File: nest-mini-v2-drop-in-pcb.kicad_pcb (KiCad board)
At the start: 4 copper layers, 74.5 x 70.6 mm, 177 parts, among them J1 1775443-2, J2 usb_c, Q1 LBSS138WT1G, Q2 BC847B, SW1 SMXS‑01K‑TP, U1 TPS62130, U10 SN74LVC125APWR, U11 MAX98357AETE_T, U12 FSUSB42MUX, U13 AP22802AW5-7, U2 MIC5365-1.8YC5-TR, U3 TPS62130, U4 MIC5365-0.9YC5-TR, U5 ESP32-S3R8, U6 W25Q128JVSIQ, U7 XU316-1024-QF60B-C24, U8 W25Q128JVSIQ, U9 TLV73333PDBVR, Y1 40MHz, Y2 24MHz

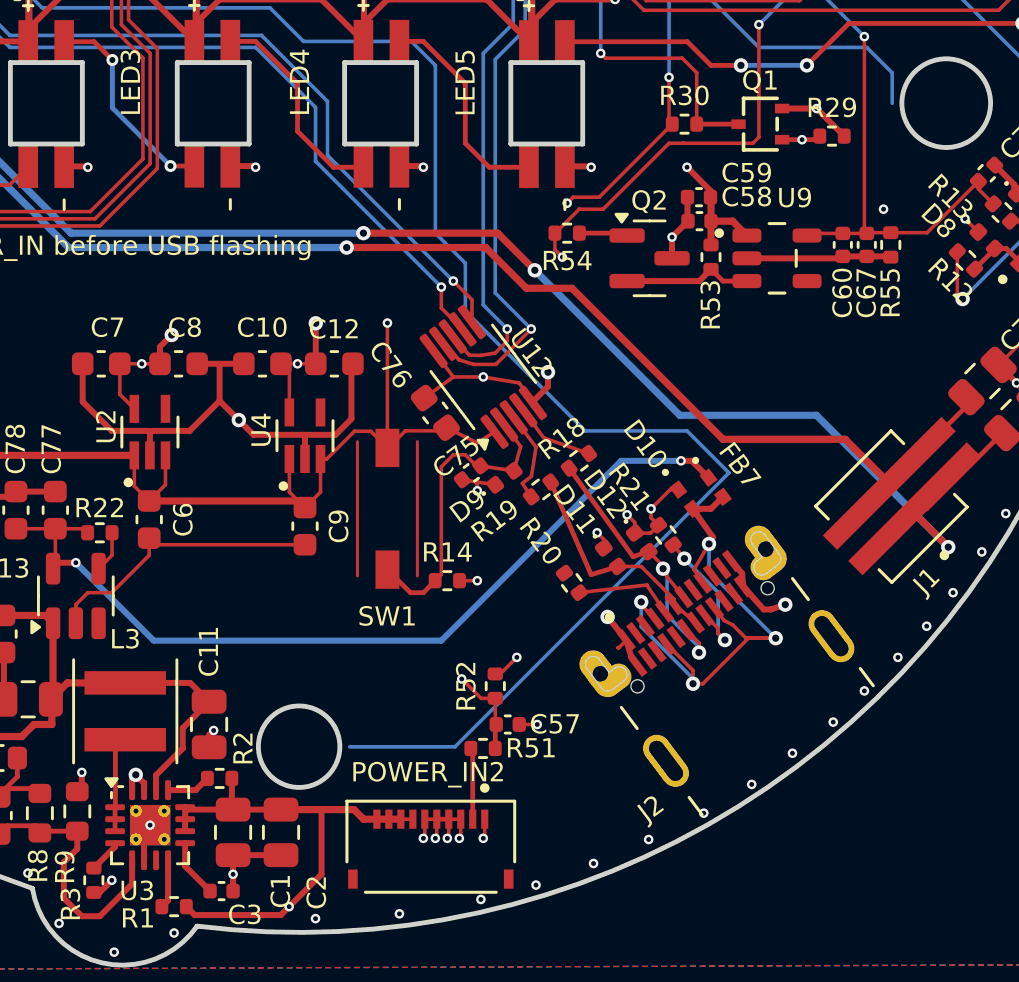
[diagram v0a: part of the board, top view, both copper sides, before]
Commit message: modifications for manufacturing
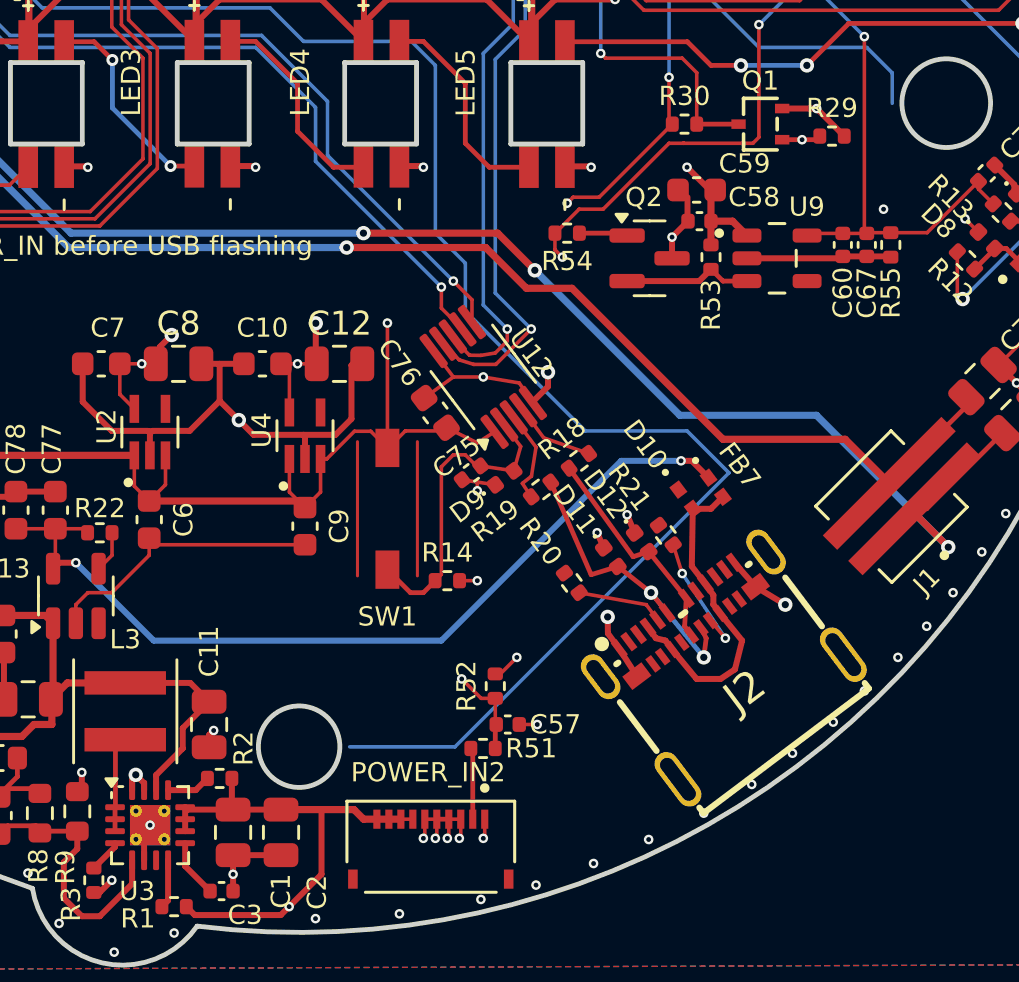
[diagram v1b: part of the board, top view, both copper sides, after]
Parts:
- C12, C8: footprint Capacitor_SMD:C_0603_1608Metric -> Capacitor_SMD:C_0805_2012Metric
- C54, C55: value 20pF -> 15pF
- C59: footprint Capacitor_SMD:C_0402_1005Metric -> Capacitor_SMD:C_0603_1608Metric
- C74: value 47uF -> 10uF
- FB7: value 0R -> 30R
- J2: footprint Onju:usb_c -> Onju:USB-C-SMD_TYPE-C-USB-18
- moved J2 0.75 mm to (153.3, 112.4)
- moved C59 0.32 mm to (152.4, 92.7)
- moved C12 0.21 mm to (137.5, 100.0)
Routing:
- net Net-(D10-A2): track 24.9 -> 13.7 mm, vias 4 -> 0
- net GND: track 202.8 -> 198.6 mm, vias 189 -> 188
- net /Power/USB_D_N: track 13.0 -> 9.37 mm, vias 2 -> 0
- net /Power/USB_D_P: track 9.67 -> 13.0 mm, vias 0 -> 2
- net Net-(J2-CC2): track 6.23 -> 5.46 mm
- net Net-(J2-CC1): track 4.17 -> 3.64 mm

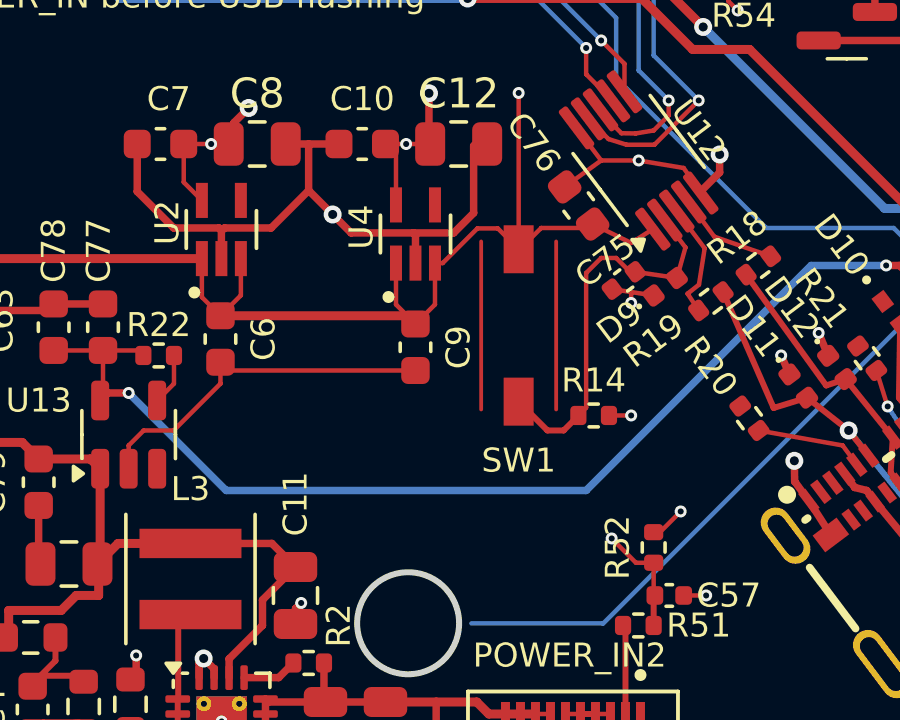
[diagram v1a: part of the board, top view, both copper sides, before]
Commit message: modifications for manufacturing
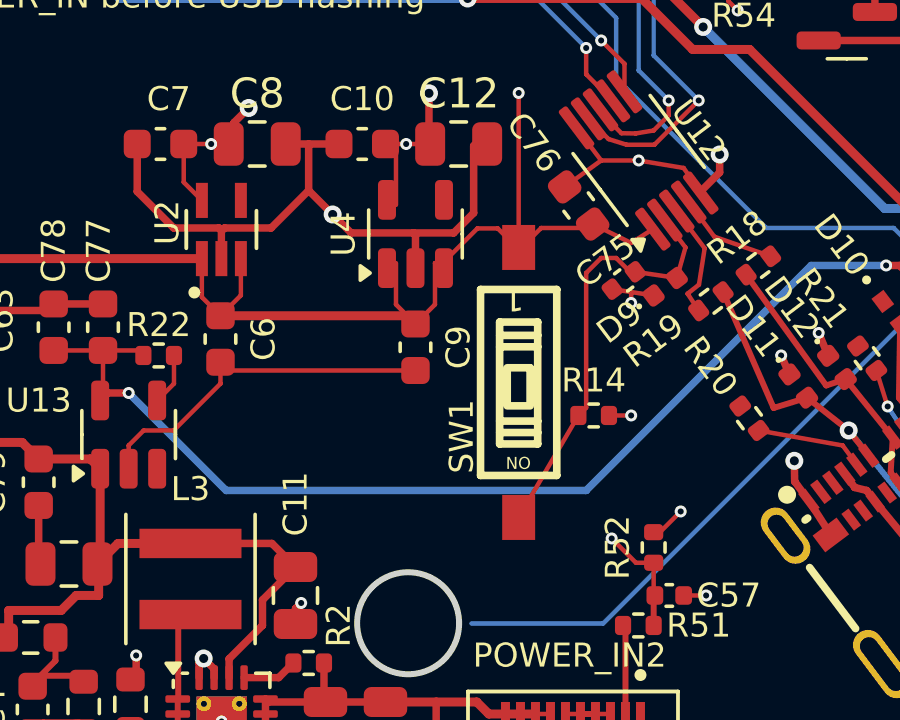
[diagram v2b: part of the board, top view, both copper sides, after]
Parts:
- SW1: value SMXS‑01K‑TP -> SMXS_01K_TP; footprint Onju:CHS-01TA -> Onju:SW-SMD_2P-L6.2-W2.5-LS9.4
- U4: value MIC5365-0.9YC5-TR -> TPS7A0309PDBVR; footprint Onju:SOT65P210X110-5N -> Package_TO_SOT_SMD:SOT-23-5
- moved SW1 1.90 mm to (139.5, 107.9), turned to -90 degrees
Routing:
- net /Power/USB_SEL: track 13.1 -> 14.4 mm

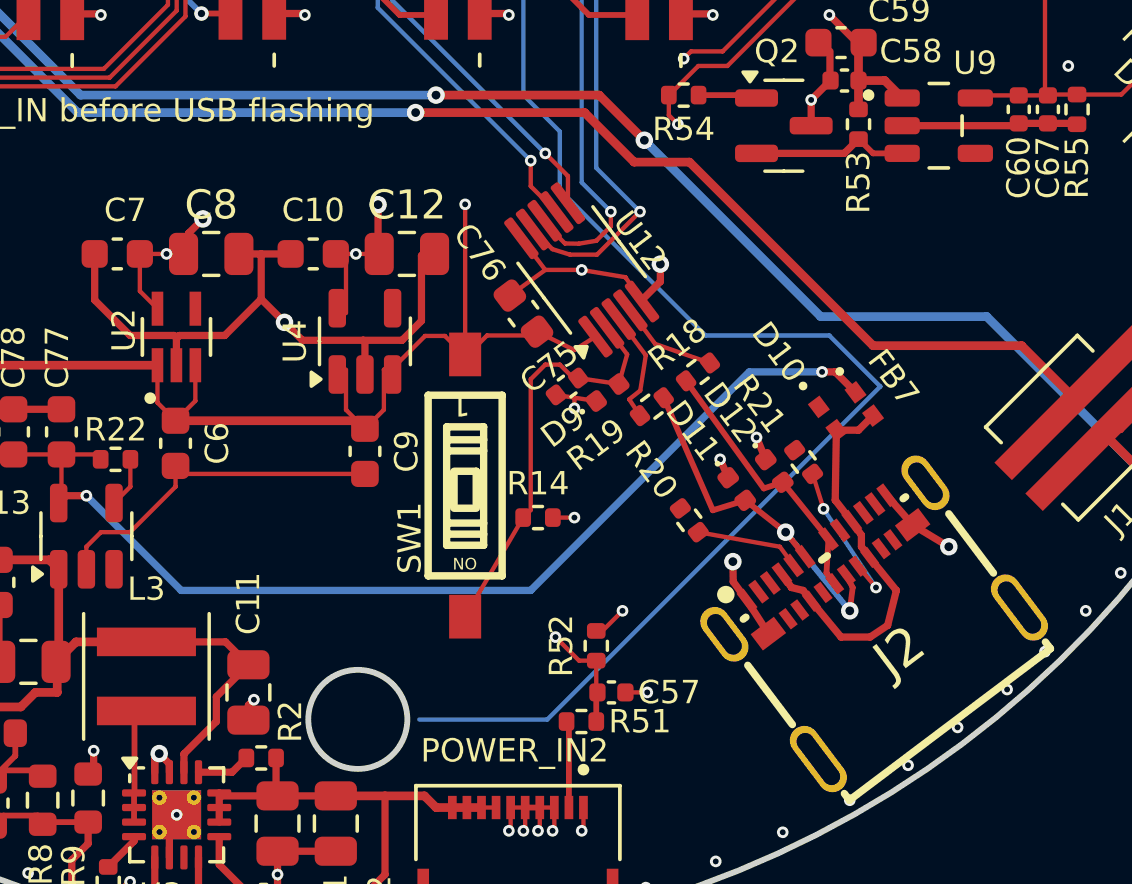
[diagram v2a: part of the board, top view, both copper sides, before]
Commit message: modifications for manufacturing
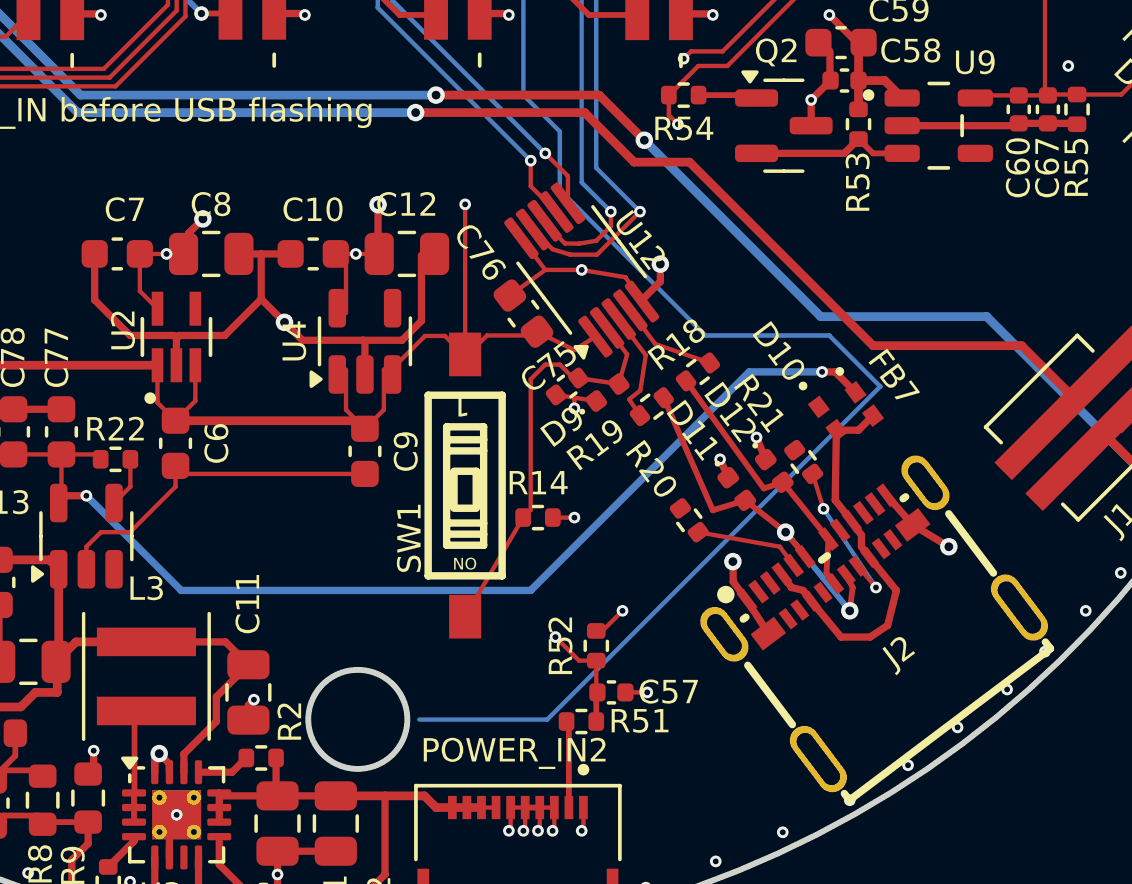
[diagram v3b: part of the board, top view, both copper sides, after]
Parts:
- MK1, MK2: value T3902 -> MMICT390200012

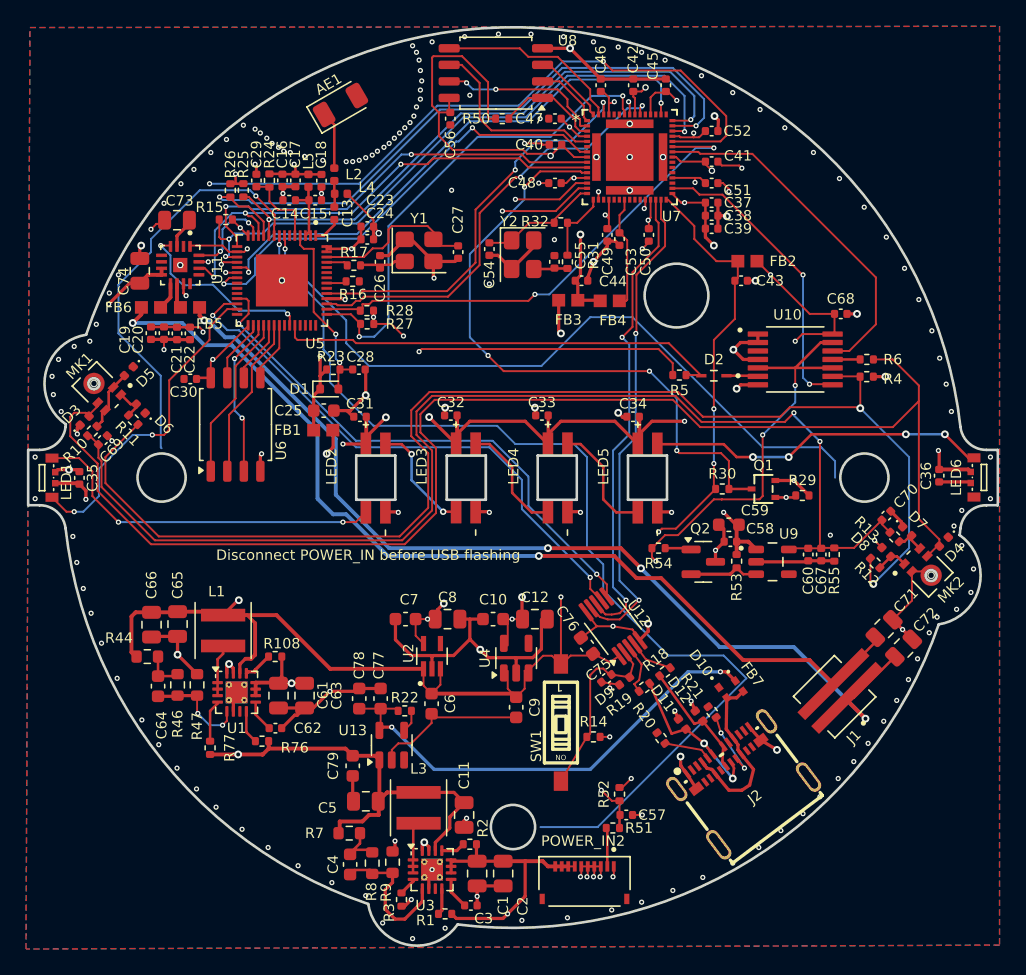
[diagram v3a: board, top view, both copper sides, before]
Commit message: modifications for manufacturing
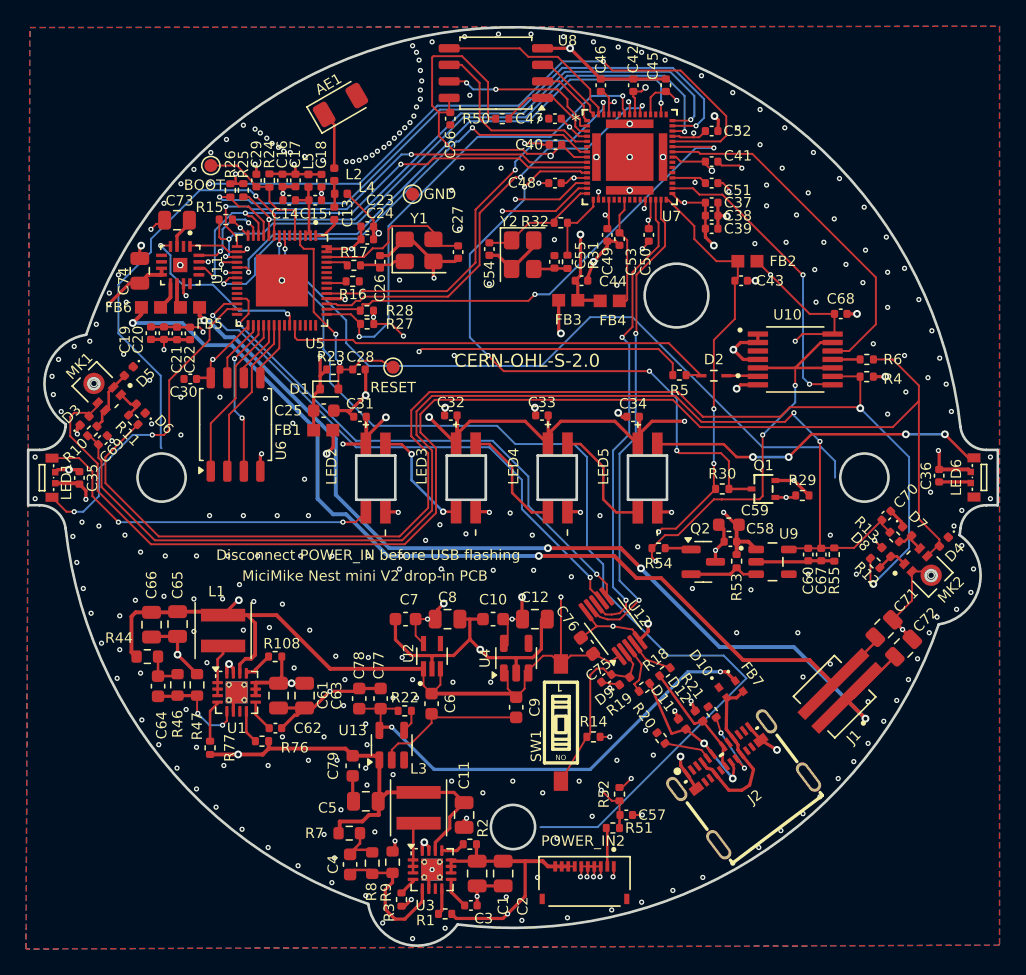
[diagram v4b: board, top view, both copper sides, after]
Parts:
- added TP1: BOOT, TestPoint:TestPoint_Pad_D1.0mm, F.Cu at (112.6, 65.1)
- added TP2: GND, TestPoint:TestPoint_Pad_D1.0mm, F.Cu at (128.1, 67.3)
- added TP3: RESET, TestPoint:TestPoint_Pad_D1.0mm, F.Cu at (126.6, 80.6)
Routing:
- net ESP_BOOT: track 6.33 -> 10.5 mm
- net ESP_RST: track 14.5 -> 18.1 mm
- net +5V: vias 11 -> 12
- net Net-(C71-Pad1): vias 2 -> 3
- net GND: vias 188 -> 318
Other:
- board text added: "CERN-OHL-S-2.0"
- board text added: "MiciMike Nest mini V2 drop-in PCB"

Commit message: modifications for manufacturing
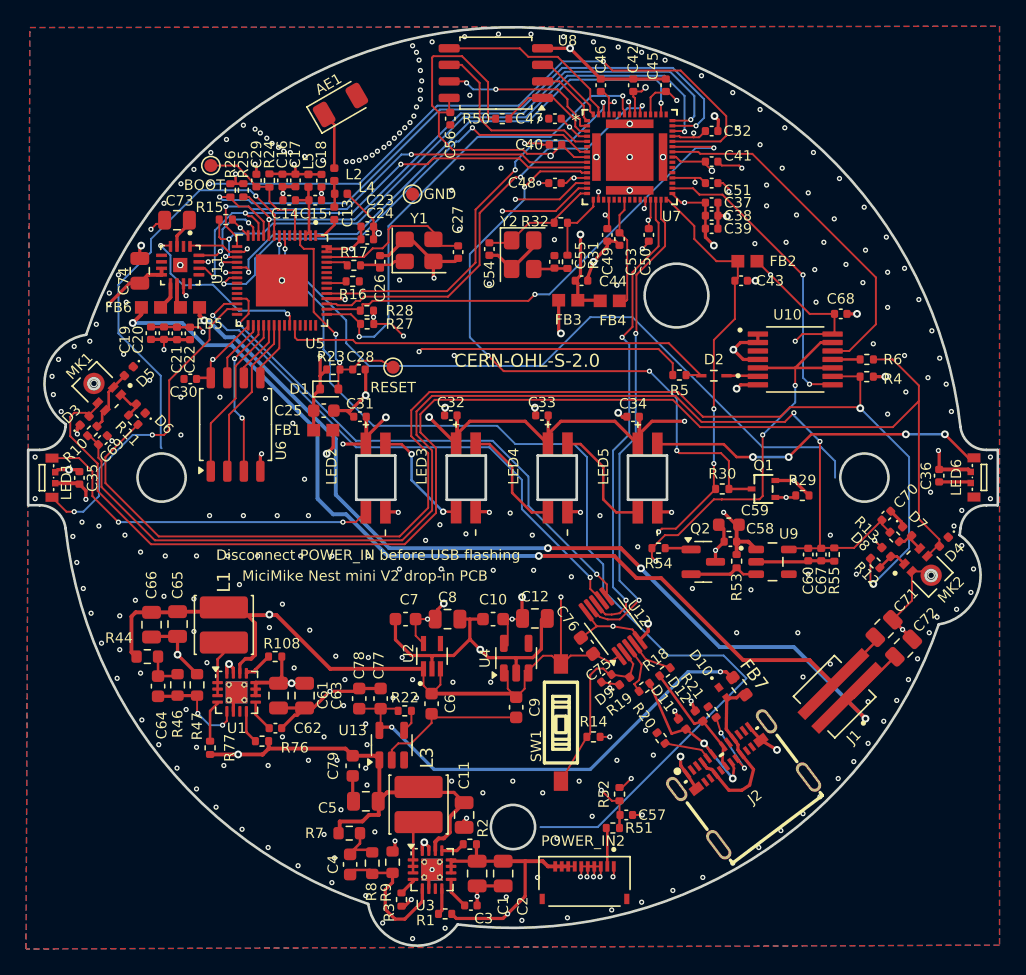
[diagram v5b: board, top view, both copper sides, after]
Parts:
- FB7: footprint Onju:TPD1E05U06DPYR -> Resistor_SMD:R_0603_1608Metric
- L1, L3: footprint Inductor_SMD:L_Coilcraft_XxL4020 -> Inductor_SMD:L_Cenker_CKCS4020
- moved L1 0.43 mm to (113.6, 100.4)
- moved L3 0.25 mm to (128.6, 114.2)
- moved C12 0.05 mm to (137.5, 99.9)
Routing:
- net +3V3: track 123.9 -> 120.6 mm
- net +5V: track 207.2 -> 207.5 mm, vias 12 -> 11
- net Net-(C71-Pad1): vias 3 -> 2
- net GND: vias 318 -> 314
